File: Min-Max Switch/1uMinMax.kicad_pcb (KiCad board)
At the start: 2 copper layers, 47 parts, among them J1 PJ301M12, J2 PJ301M12, J3 PJ301M12, J4 PJ301M12, J5 PJ301M12, J6 PJ301M12, J7 PJ301M12, J8 PJ301M12, P1 CONN_01X03, U1 TL074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

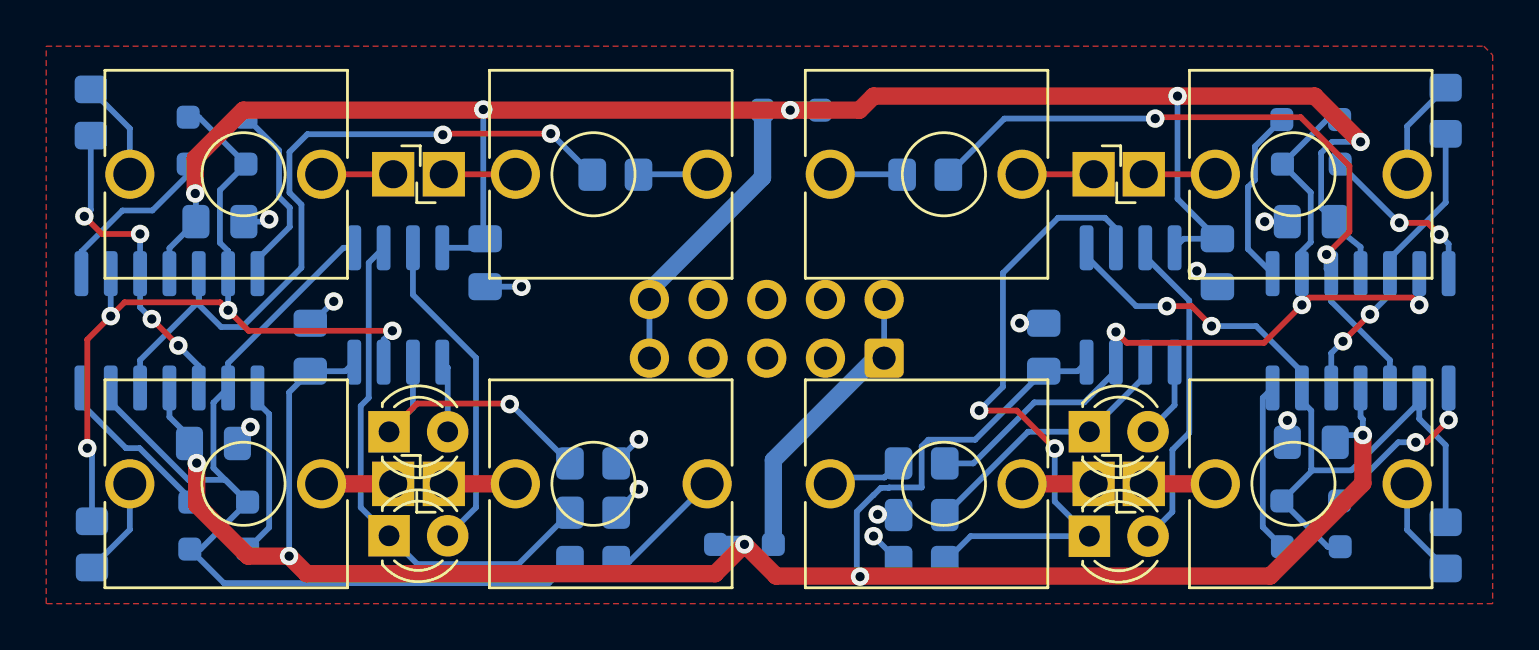
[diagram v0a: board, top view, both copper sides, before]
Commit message: Updated sub-dom switch circuit. It now clones a section of the Mutable Instruments Kinks circuit
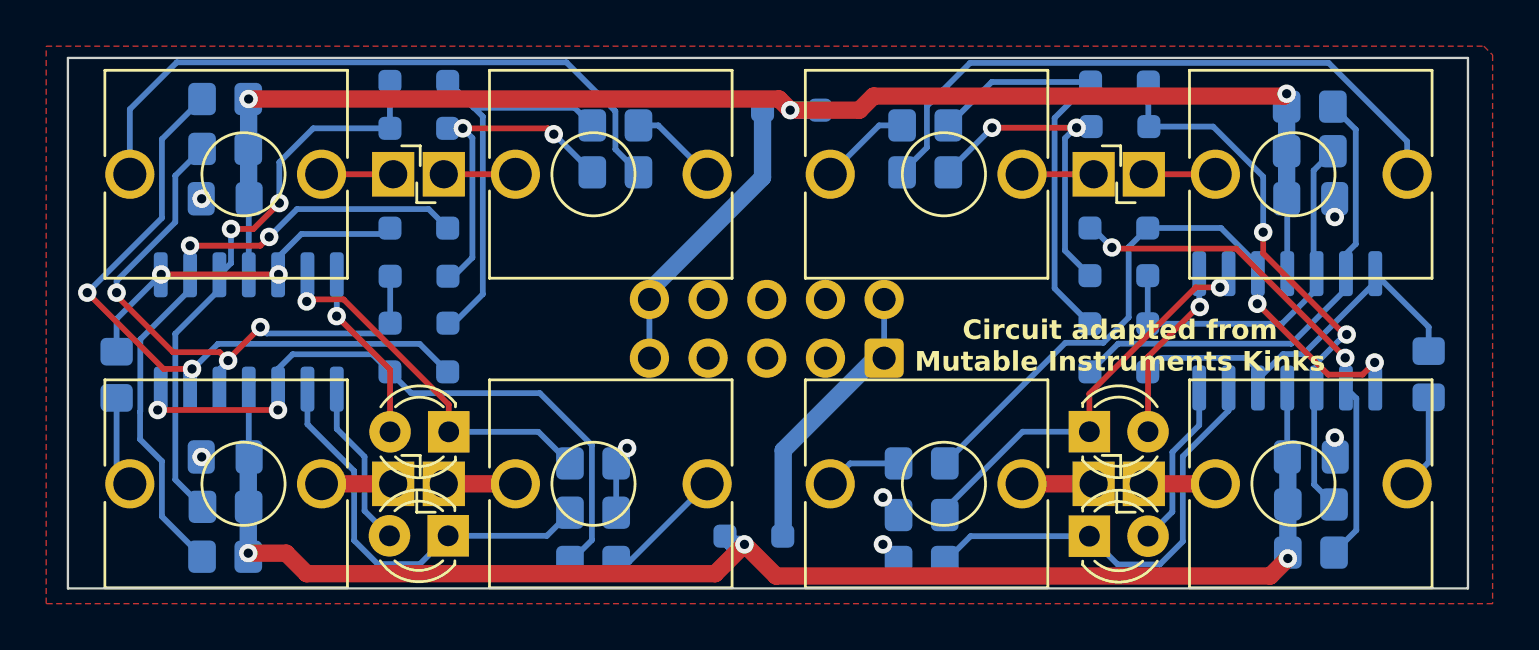
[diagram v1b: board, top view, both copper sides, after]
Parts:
- removed C5, C6, C7, C8: 100n, Capacitor_SMD:C_0805_2012Metric_Pad1.18x1.45mm_HandSolder
- removed U3, U4: TL072, Package_SO:SOIC-8_3.9x4.9mm_P1.27mm
- added D15: LL4148, Diode_SMD:D_SOD-323_HandSoldering, B.Cu at (145.5, 99.8)
- added D16: LL4148, Diode_SMD:D_SOD-323_HandSoldering, B.Cu at (145.5, 97.7)
- added D17: LL4148, Diode_SMD:D_SOD-323_HandSoldering, B.Cu at (145.5, 95.6)
- added D18: LL4148, Diode_SMD:D_SOD-323_HandSoldering, B.Cu at (145.5, 101.9)
- added R13: 220k, Resistor_SMD:R_0805_2012Metric_Pad1.20x1.40mm_HandSolder, B.Cu at (106.8, 107.7)
- added R14: 220k, Resistor_SMD:R_0805_2012Metric_Pad1.20x1.40mm_HandSolder, B.Cu at (106.8, 109.9)
- added R15: 220k, Resistor_SMD:R_0805_2012Metric_Pad1.20x1.40mm_HandSolder, B.Cu at (106.8, 92.2)
- added R16: 220k, Resistor_SMD:R_0805_2012Metric_Pad1.20x1.40mm_HandSolder, B.Cu at (106.8, 90.0)
- added R17: 220k, Resistor_SMD:R_0805_2012Metric_Pad1.20x1.40mm_HandSolder, B.Cu at (153.8, 107.6)
- added R18: 220k, Resistor_SMD:R_0805_2012Metric_Pad1.20x1.40mm_HandSolder, B.Cu at (153.8, 92.3)
- added R19: 220k, Resistor_SMD:R_0805_2012Metric_Pad1.20x1.40mm_HandSolder, B.Cu at (153.8, 109.7)
- added R20: 220k, Resistor_SMD:R_0805_2012Metric_Pad1.20x1.40mm_HandSolder, B.Cu at (153.8, 90.4)
- R10, R11, R12, R9: value R -> RL
- moved C1 43.0 mm to (106.8, 94.4), turned to 180 degrees
- moved D6 39.7 mm to (115.2, 101.9)
- moved D5 39.6 mm to (115.2, 99.7)
- moved C2 35.7 mm to (106.8, 105.5), turned to 0 degrees
- moved R1 22.9 mm to (123.7, 93.2), turned to 180 degrees
- moved R6 22.7 mm to (137.1, 93.2), turned to 0 degrees
- moved D8 20.0 mm to (145.5, 91.2), turned to 180 degrees
- moved D7 19.9 mm to (145.5, 89.3)
- moved D3 16.4 mm to (115.2, 95.6)
- moved D4 13.1 mm to (115.2, 97.7), turned to 180 degrees
- moved D1 8.87 mm to (115.2, 91.3), turned to 0 degrees
- moved D2 8.87 mm to (115.2, 89.3)
- moved R8 7.44 mm to (158.9, 102.0)
- moved R3 7.42 mm to (102.1, 102.0)
- moved U1 3.43 mm to (107.8, 100.1)
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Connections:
- D4 pad 1: Net-(D4-K) -> Net-(D1-A)
- D4 pad 2: Net-(D3-A) -> Net-(D4-A)
- D5 pad 1: Net-(D5-K) -> Net-(D2-A)
- D5 pad 2: Net-(D5-A) -> Net-(D4-A)
- D6 pad 1: Net-(D5-K) -> Net-(D6-K)
- D7 pad 2: Net-(D7-A) -> Net-(D15-K)
- D8 pad 1: Net-(D8-K) -> Net-(D7-K)
- D8 pad 2: Net-(D7-A) -> Net-(D16-K)
- R1 pad 2: Net-(U1A-+) -> Net-(D1-A)
- R2 pad 2: Net-(U1B-+) -> Net-(D2-A)
- R3 pad 1: Net-(D1-K) -> Net-(D3-A)
- R4 pad 1: Net-(D3-A) -> Net-(D6-K)
- R5 pad 2: Net-(U2A-+) -> Net-(D15-K)
- R6 pad 2: Net-(U2B-+) -> Net-(D16-K)
- R7 pad 1: Net-(D5-K) -> Net-(D17-A)
- R8 pad 1: Net-(D7-A) -> Net-(D18-K)
- U1 pad 1: Net-(D1-A) -> Net-(D3-A)
- U1 pad 10: Net-(U1A-+) -> Net-(D6-K)
- U1 pad 12: Net-(U1B-+) -> Net-(D4-A)
- U1 pad 13: Net-(D3-A) -> Net-(D6-A)
- U1 pad 14: Net-(D4-K) -> Net-(D6-K)
- U1 pad 2: Net-(D1-K) -> Net-(D3-K)
- U1 pad 3: Net-(U1A-+) -> Net-(D1-K)
- U1 pad 5: Net-(U1B-+) -> Net-(D3-A)
- U1 pad 6: Net-(D1-K) -> Net-(D9-KA)
- U1 pad 7: Net-(D2-A) -> Net-(D9-AK)
- U1 pad 8: Net-(D3-K) -> Net-(D10-AK)
- U1 pad 9: Net-(D3-A) -> Net-(D10-KA)
- U2 pad 1: Net-(D5-A) -> Net-(D11-AK)
- U2 pad 10: Net-(U2A-+) -> Net-(D7-K)
- U2 pad 12: Net-(U2B-+) -> Net-(D18-K)
- U2 pad 13: Net-(D7-A) -> Net-(D12-KA)
- U2 pad 14: Net-(D8-K) -> Net-(D12-AK)
- U2 pad 2: Net-(D5-K) -> Net-(D11-KA)
- U2 pad 3: Net-(U2A-+) -> Net-(D17-A)
- U2 pad 5: Net-(U2B-+) -> Net-(D15-A)
- U2 pad 6: Net-(D5-K) -> Net-(D18-A)
- U2 pad 7: Net-(D6-A) -> Net-(D18-K)
- U2 pad 8: Net-(D7-K) -> Net-(D17-A)
- U2 pad 9: Net-(D7-A) -> Net-(D17-K)
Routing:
- net Net-(D5-K): track 35.2 -> 0.00 mm, vias 3 -> 0
- net Net-(U1B-+): track 32.7 -> 0.00 mm, vias 2 -> 0
- net Net-(D7-A): track 31.9 -> 0.00 mm, vias 2 -> 0
- net -12V: track 92.9 -> 62.2 mm, vias 5 -> 3
- net Net-(U2A-+): track 30.4 -> 0.00 mm, vias 2 -> 0
- net Net-(D17-A): track 0.00 -> 29.2 mm, vias 0 -> 2
- net Net-(D3-A): track 42.9 -> 14.2 mm, vias 0 -> 2
- net Net-(D6-K): track 0.00 -> 27.0 mm, vias 0 -> 2
- net Net-(D4-A): track 0.00 -> 25.2 mm, vias 0 -> 3
- net Net-(J1-Pad3): track 4.37 -> 28.6 mm
- net Net-(J6-Pad3): track 4.44 -> 27.7 mm
- net Net-(D17-K): track 0.00 -> 22.3 mm, vias 0 -> 2
- net Net-(D6-A): track 7.41 -> 28.5 mm
- net +12V: track 83.1 -> 62.1 mm, vias 5 -> 3
- net Net-(D18-A): track 0.00 -> 20.4 mm
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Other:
- board outline added: 60.6 x 23 mm
- board text added: "Circuit adapted from Mutable Instruments Kinks"
- board text added: "schottky"
- board text removed: "K"

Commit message: Updated diode silkscreen
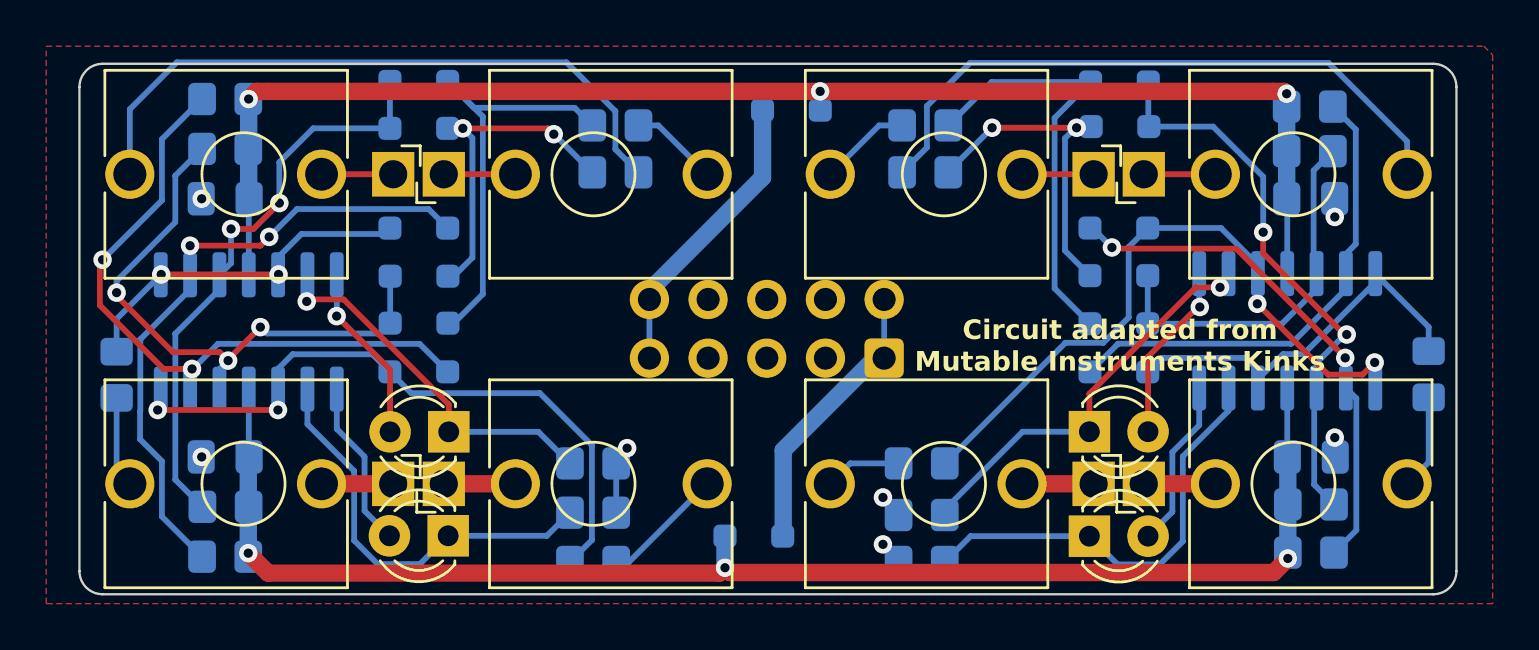
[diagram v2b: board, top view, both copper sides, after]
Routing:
- net +12V: track 62.1 -> 61.3 mm
- net -12V: track 62.2 -> 61.5 mm
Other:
- board size 60.6 x 23 mm -> 59.6 x 23 mm
